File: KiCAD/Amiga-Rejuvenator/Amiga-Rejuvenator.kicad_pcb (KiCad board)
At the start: 4 copper layers, 241.8 x 174.8 mm, 120 parts, among them J1 GND, J15 28M, J17 RMBCLKS, J18 GND, J19 +12X, U1 74LS245, U10 V53C104, U11 V53C104, U12 V53C104, U13 V53C104, U14 74LS244-U16,U17, U15 74LS373, U16 74LS244-U16,U17, U17 74LS244-U16,U17, U18 512K-ROM, U19 8372-FatAgnus, U19B1 8361-Agnus-Socket, U2 74LS393-U2, U20 8364-Paula, U20B1 8364-Paula-Socket, U21 74LS245, U22 74LS245, U23 RP, U24 RP, U25 8362-Denise, U25B1 8362-Denise-Socket, U26 74HC245, U27 OKI6242B, U28 PAL16L8, U29 PAL16L8, U3 74F257, U30 PAL20L8, U31 PAL20L8, U32 74LS74, U33 74LS04, U34 74HC245, U35 74F257, U36 PALCAS, U37 PALEN, U38 U3I, U39 U3G, U4 74LS244-U16,U17, U40 U2J, U41 U2I, U5 74LS373, U6 V53C104, U7 V53C104, U8 V53C104, U9 V53C104, X1 X1, X14 X14, X15 X15, X16 VideoSlot 1, X17 VideoSlot 2, Y1 Crystal

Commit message: Remove redundant traces
Remove redundant power traces which were embedded in a fill zone.
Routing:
- net GND: track 588.4 -> 562.8 mm
- net +5V: track 345.8 -> 332.8 mm

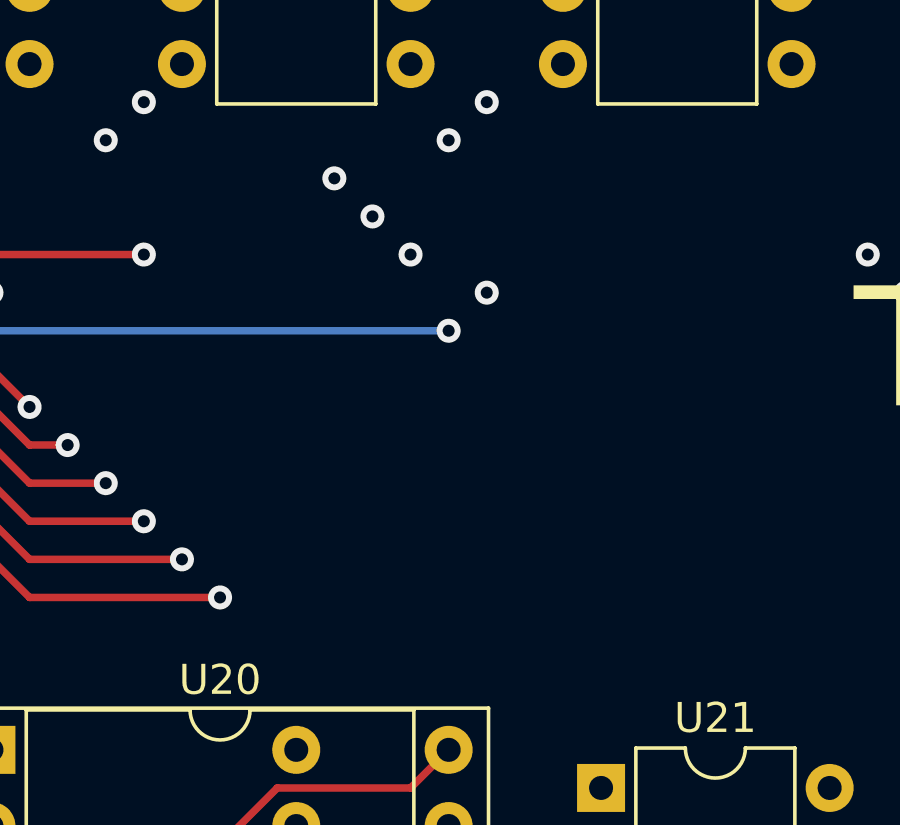
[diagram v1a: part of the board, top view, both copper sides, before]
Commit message: Restore Logo to PCB Artwork
The logo was inadvertently missing from the board artwork.
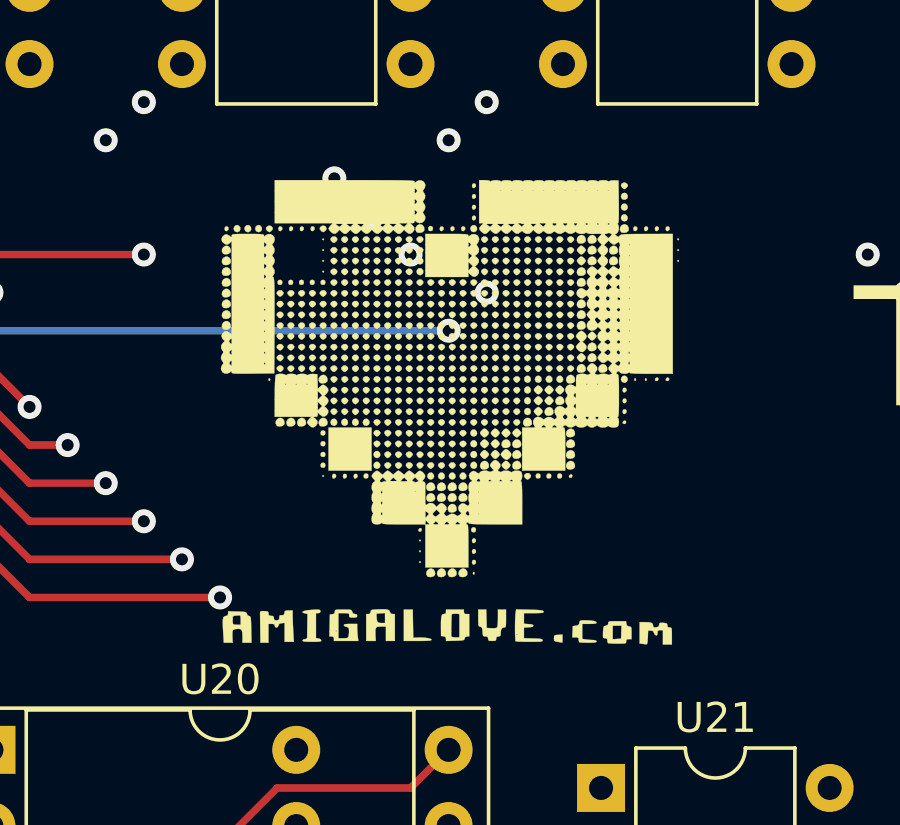
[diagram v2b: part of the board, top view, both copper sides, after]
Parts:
- added G***: LOGO, rejuvenator_positions:Untitled, F.Cu at (232.4, 101.6)
